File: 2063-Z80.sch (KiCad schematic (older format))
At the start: 80 parts, among them J1 Conn_01x05, J10 Conn_01x07, J11 Conn_02x03_Odd_Even, J2 DM3D-SF(41), J3 Conn_02x20_Counter_Clockwise, J4 Conn_02x05_Odd_Even, J5 Conn_02x05_Odd_Even, J6 0548190519, J7 Conn_02x13_Top_Bottom, J8 Conn_01x05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

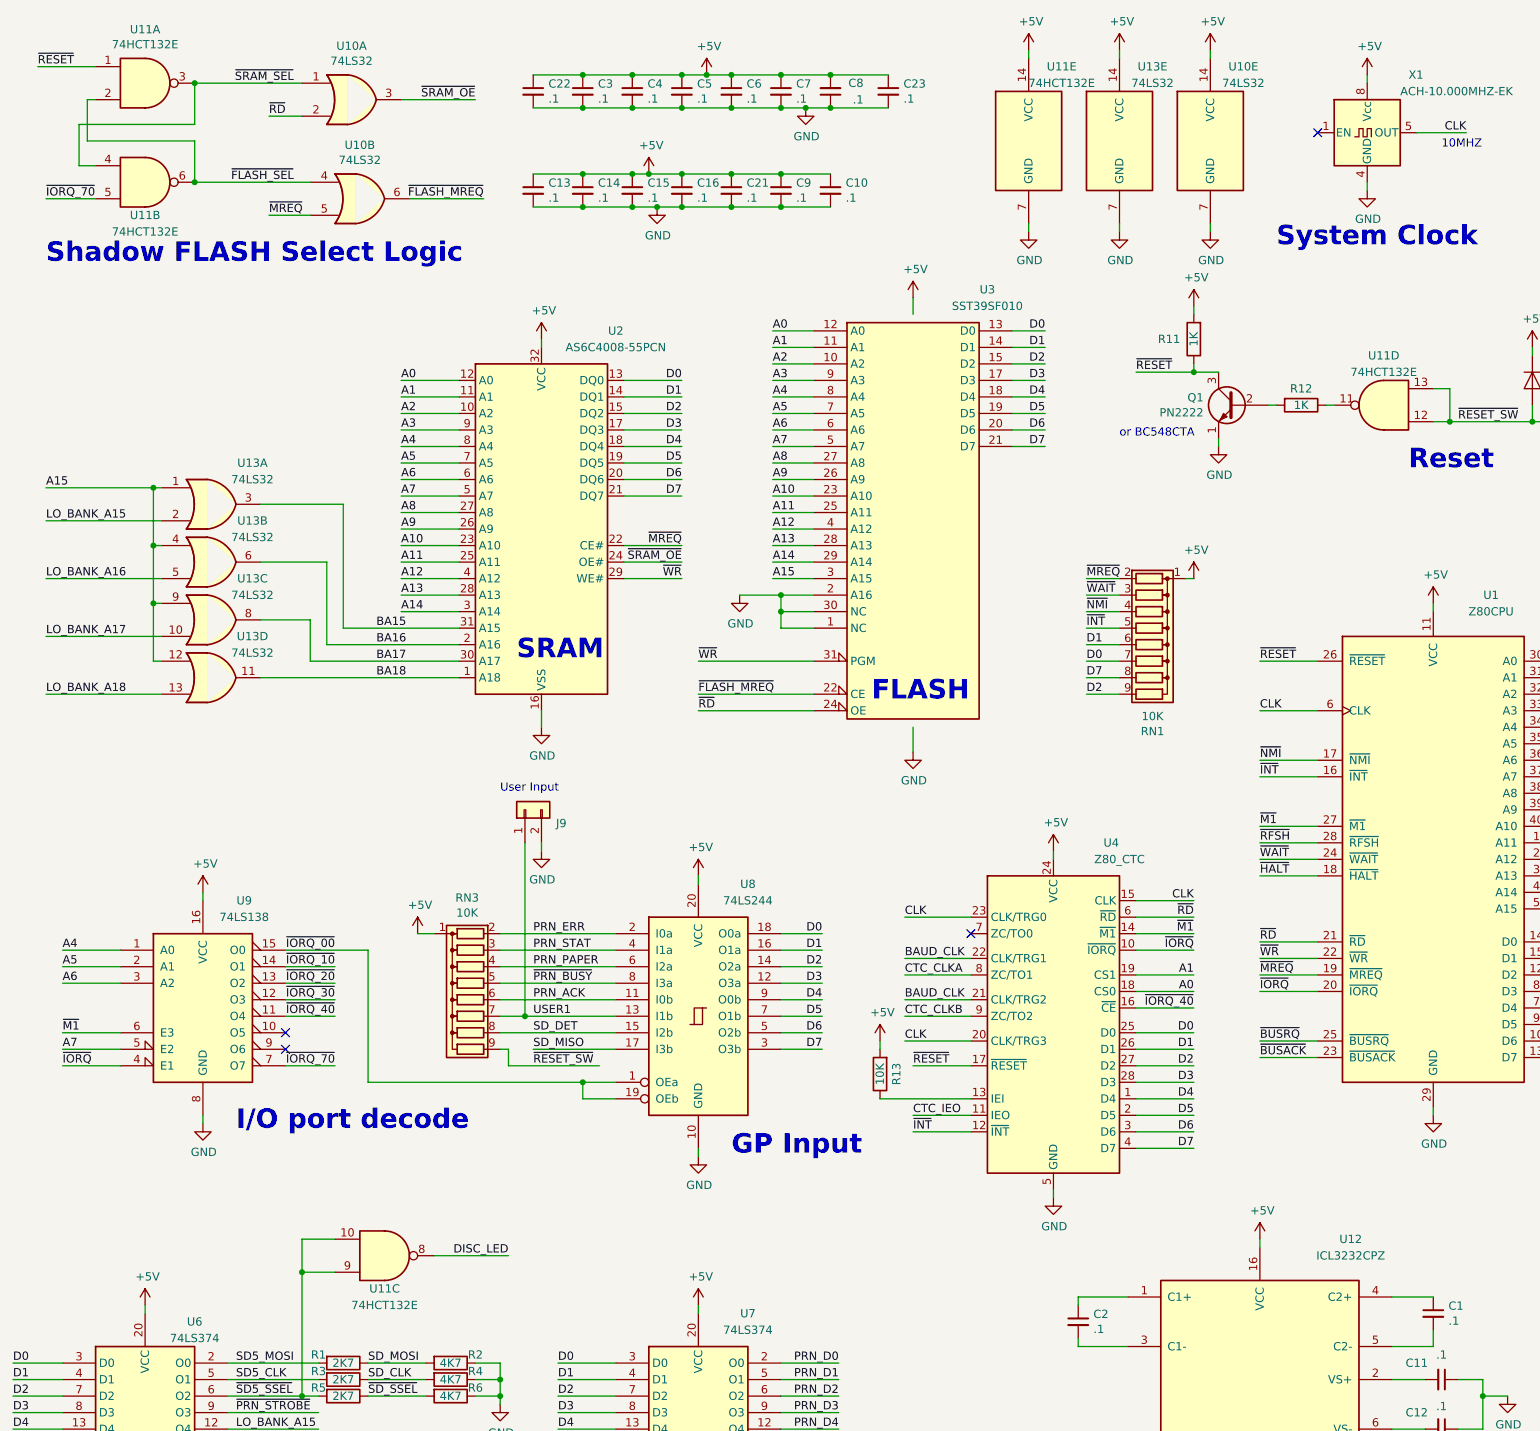
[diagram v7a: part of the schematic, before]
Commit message: Change U11 symbol to a Schmitt NAND
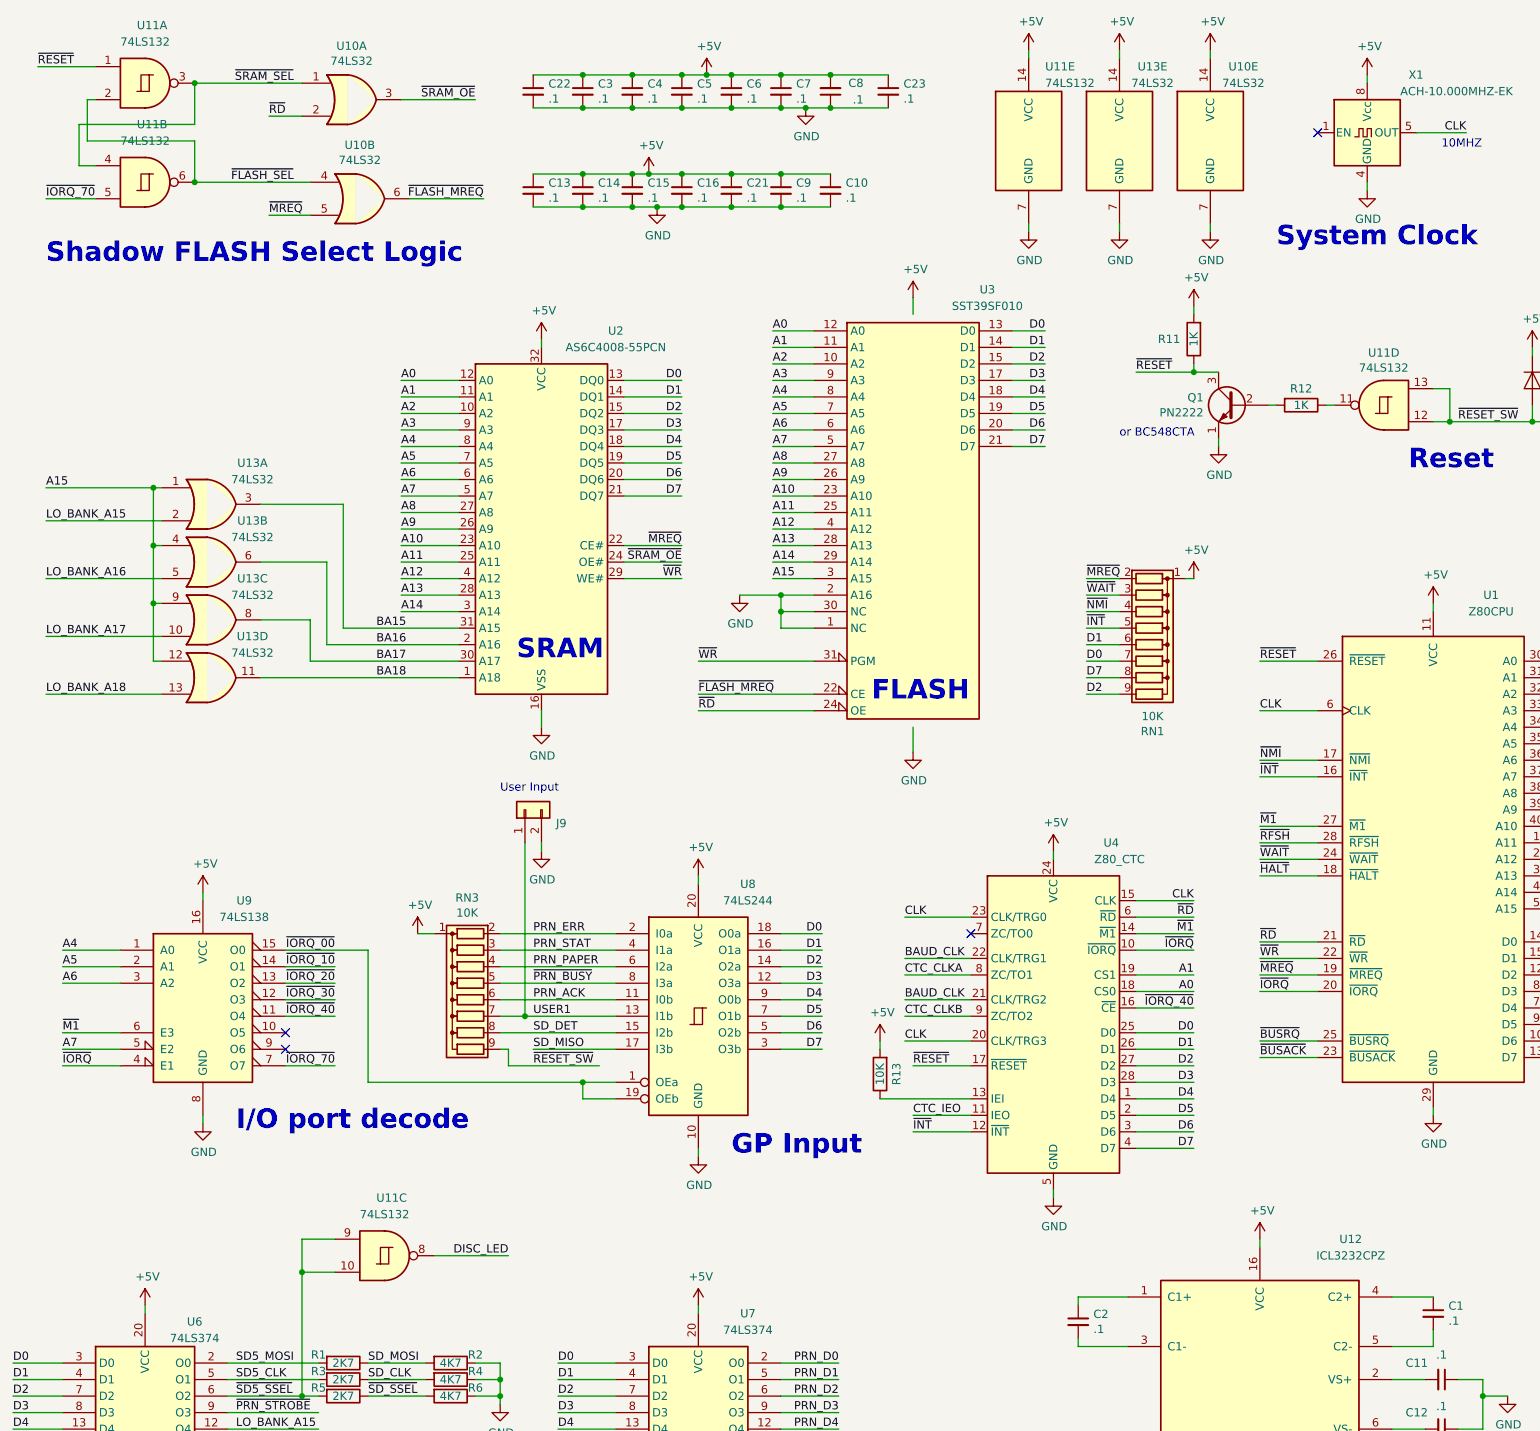
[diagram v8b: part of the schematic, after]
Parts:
- removed U11: 74HCT132E, Package_DIP:DIP-14_W7.62mm_Socket, symbol 74xx:7400
- added U11: 74LS132, Package_DIP:DIP-14_W7.62mm_Socket, symbol 74xx:74LS132
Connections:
- net +5V: now also U11.14 (VCC)
- net DISC_LED: now also U11.8
- net GND: now also U11.7 (GND)
- net ~FLASH_SEL: now also U11.2, U11.6
- net ~IORQ_70: now also U11.5
- net ~RESET: now also U11.1
- net ~RESET_SW: now also U11.12, U11.13
- net ~SD5_SSEL: now also U11.10, U11.9
- net ~SRAM_SEL: now also U11.3, U11.4
- net at R12.1: now also U11.11
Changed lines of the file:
@@
 Text Notes 750  2000 0    118  ~ 24
 Shadow FLASH Select Logic
-Connection ~ 1650 900
 Text Label 2250 900  2    50   ~ 0
 ~SRAM_SEL
 Text Label 2250 1500 2    50   ~ 0
 ~FLASH_SEL
-Connection ~ 1650 1500
 Text Notes 5750 4650 0    118  ~ 24
 FLASH
@@
 Connection ~ 10600 2950
 $Comp
-L 74xx:7400 U11
-U 1 1 61038EB5
-P 1350 900
-F 0 "U11" H 1350 1225 50  0000 C CNN
-F 1 "74HCT132E" H 1350 1134 50  0000 C CNN
-F 2 "Package_DIP:DIP-14_W7.62mm_Socket" H 1350 900 50  0001 C CNN
-F 3 "http://www.ti.com/lit/gpn/sn7400" H 1350 900 50  0001 C CNN
-F 4 "296-1626-ND‎" H 1350 900 50  0001 C CNN "Digi-Key_PN"
-F 5 "SN74LS00N‎" H 1350 900 50  0001 C CNN "MPN"
-	1    1350 900
-	1    0    0    -1
-$EndComp
-$Comp
-L 74xx:7400 U11
-U 2 1 6103B52C
-P 1350 1500
-F 0 "U11" H 1350 1300 50  0000 C CNN
-F 1 "74HCT132E" H 1350 1200 50  0000 C CNN
-F 2 "Package_DIP:DIP-14_W7.62mm_Socket" H 1350 1500 50  0001 C CNN
-F 3 "http://www.ti.com/lit/gpn/sn7400" H 1350 1500 50  0001 C CNN
-F 4 "296-1626-ND‎" H 1350 1500 50  0001 C CNN "Digi-Key_PN"
-F 5 "SN74LS00N‎" H 1350 1500 50  0001 C CNN "MPN"
-	2    1350 1500
-	1    0    0    -1
-$EndComp
-$Comp
 L 74xx:74LS32 U10
 U 1 1 6103CA65
@@
 $EndComp
 $Comp
-L 74xx:7400 U11
-U 5 1 61CF1304
-P 6700 1250
-F 0 "U11" H 6900 1700 50  0000 C CNN
-F 1 "74HCT132E" H 6900 1600 50  0000 C CNN
-F 2 "Package_DIP:DIP-14_W7.62mm_Socket" H 6700 1250 50  0001 C CNN
-F 3 "http://www.ti.com/lit/gpn/sn7400" H 6700 1250 50  0001 C CNN
-F 4 "296-1626-ND‎" H 6700 1250 50  0001 C CNN "Digi-Key_PN"
-F 5 "SN74LS00N‎" H 6700 1250 50  0001 C CNN "MPN"
-	5    6700 1250
-	1    0    0    -1
-$EndComp
-$Comp
 L Connector_Generic:Conn_02x13_Top_Bottom J7
 U 1 1 614C2C3B
@@
 $EndComp
 $Comp
-L 74xx:7400 U11
-U 4 1 61729047
-P 8850 2850
-F 0 "U11" H 8850 2550 50  0000 C CNN
-F 1 "74HCT132E" H 8850 2650 50  0000 C CNN
-F 2 "Package_DIP:DIP-14_W7.62mm_Socket" H 8850 2850 50  0001 C CNN
-F 3 "http://www.ti.com/lit/gpn/sn7400" H 8850 2850 50  0001 C CNN
-F 4 "296-1626-ND‎" H 8850 2850 50  0001 C CNN "Digi-Key_PN"
-F 5 "SN74LS00N‎" H 8850 2850 50  0001 C CNN "MPN"
-	4    8850 2850
-	-1   0    0    1
-$EndComp
-$Comp
 L Oscillator:CXO_DIP8 X2
 U 1 1 61461749
@@
 $EndComp
 $Comp
-L 74xx:7400 U11
-U 3 1 61726D47
-P 2800 8000
-F 0 "U11" H 2800 8200 50  0000 C CNN
-F 1 "74HCT132E" H 2800 8300 50  0000 C CNN
-F 2 "Package_DIP:DIP-14_W7.62mm_Socket" H 2800 8000 50  0001 C CNN
-F 3 "http://www.ti.com/lit/gpn/sn7400" H 2800 8000 50  0001 C CNN
-F 4 "296-1626-ND‎" H 2800 8000 50  0001 C CNN "Digi-Key_PN"
-F 5 "SN74LS00N‎" H 2800 8000 50  0001 C CNN "MPN"
-	3    2800 8000
-	1    0    0    1
-$EndComp
-$Comp
 L Connector_Generic:Conn_02x03_Odd_Even J11
 U 1 1 6162E995
@@
 Text Notes 3500 5200 0    50   ~ 0
 User Input
+$Comp
+L 74xx:74LS132 U11
+U 4 1 61B0DD06
+P 8850 2850
+F 0 "U11" H 8850 2533 50  0000 C CNN
+F 1 "74LS132" H 8850 2624 50  0000 C CNN
+F 2 "Package_DIP:DIP-14_W7.62mm_Socket" H 8850 2850 50  0001 C CNN
+F 3 "http://www.ti.com/lit/gpn/sn74LS132" H 8850 2850 50  0001 C CNN
+F 4 "‎SN74LS132N‎" H 8850 2850 50  0001 C CNN "Description"
+F 5 "296-3645-5-ND‎" H 8850 2850 50  0001 C CNN "Digi-Key_PN"
+	4    8850 2850
+	-1   0    0    1
+$EndComp
+$Comp
+L 74xx:74LS132 U11
+U 5 1 61B1D6A7
+P 6700 1250
+F 0 "U11" H 6800 1700 50  0000 L CNN
+F 1 "74LS132" H 6800 1600 50  0000 L CNN
+F 2 "Package_DIP:DIP-14_W7.62mm_Socket" H 6700 1250 50  0001 C CNN
+F 3 "http://www.ti.com/lit/gpn/sn74LS132" H 6700 1250 50  0001 C CNN
+F 4 "‎SN74LS132N‎" H 6700 1250 50  0001 C CNN "Description"
+F 5 "296-3645-5-ND‎" H 6700 1250 50  0001 C CNN "Digi-Key_PN"
+	5    6700 1250
+	1    0    0    -1
+$EndComp
+$Comp
+L 74xx:74LS132 U11
+U 1 1 61B44F97
+P 1350 900
+F 0 "U11" H 1300 1250 50  0000 L CNN
+F 1 "74LS132" H 1200 1150 50  0000 L CNN
+F 2 "Package_DIP:DIP-14_W7.62mm_Socket" H 1350 900 50  0001 C CNN
+F 3 "http://www.ti.com/lit/gpn/sn74LS132" H 1350 900 50  0001 C CNN
+F 4 "‎SN74LS132N‎" H 1350 900 50  0001 C CNN "Description"
+F 5 "296-3645-5-ND‎" H 1350 900 50  0001 C CNN "Digi-Key_PN"
+	1    1350 900
+	1    0    0    -1
+$EndComp
+Connection ~ 1650 900
+$Comp
+L 74xx:74LS132 U11
+U 2 1 61BA3090
+P 1350 1500
+F 0 "U11" H 1300 1850 50  0000 L CNN
+F 1 "74LS132" H 1200 1750 50  0000 L CNN
+F 2 "Package_DIP:DIP-14_W7.62mm_Socket" H 1350 1500 50  0001 C CNN
+F 3 "http://www.ti.com/lit/gpn/sn74LS132" H 1350 1500 50  0001 C CNN
+F 4 "‎SN74LS132N‎" H 1350 1500 50  0001 C CNN "Description"
+F 5 "296-3645-5-ND‎" H 1350 1500 50  0001 C CNN "Digi-Key_PN"
+	2    1350 1500
+	1    0    0    -1
+$EndComp
+Connection ~ 1650 1500
+$Comp
+L 74xx:74LS132 U11
+U 3 1 61BB7959
+P 2800 8000
+F 0 "U11" H 2750 8350 50  0000 L CNN
+F 1 "74LS132" H 2650 8250 50  0000 L CNN
+F 2 "Package_DIP:DIP-14_W7.62mm_Socket" H 2800 8000 50  0001 C CNN
+F 3 "http://www.ti.com/lit/gpn/sn74LS132" H 2800 8000 50  0001 C CNN
+F 4 "‎SN74LS132N‎" H 2800 8000 50  0001 C CNN "Description"
+F 5 "296-3645-5-ND‎" H 2800 8000 50  0001 C CNN "Digi-Key_PN"
+	3    2800 8000
+	1    0    0    -1
+$EndComp
 $EndSCHEMATC
